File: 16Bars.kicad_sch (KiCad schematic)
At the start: 34 parts, among them IC1 CD4033BE, IC2 CD4033BE, IC3 CD4510BE, J1 CLOCK_IN, J2 Conn_02x05_Odd_Even, Q1 2N3904, Q2 2N3904, Q3 2N3904, Q4 2N3904, Q5 2N3904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

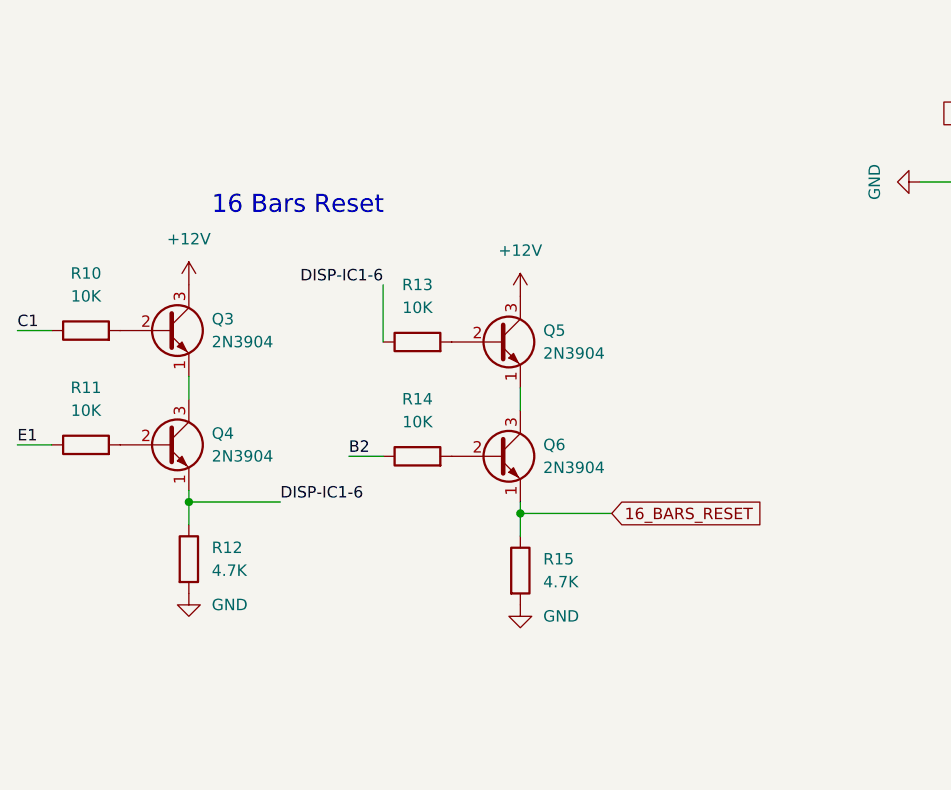
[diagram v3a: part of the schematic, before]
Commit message: Fix transistor logic. TODO resistor values.
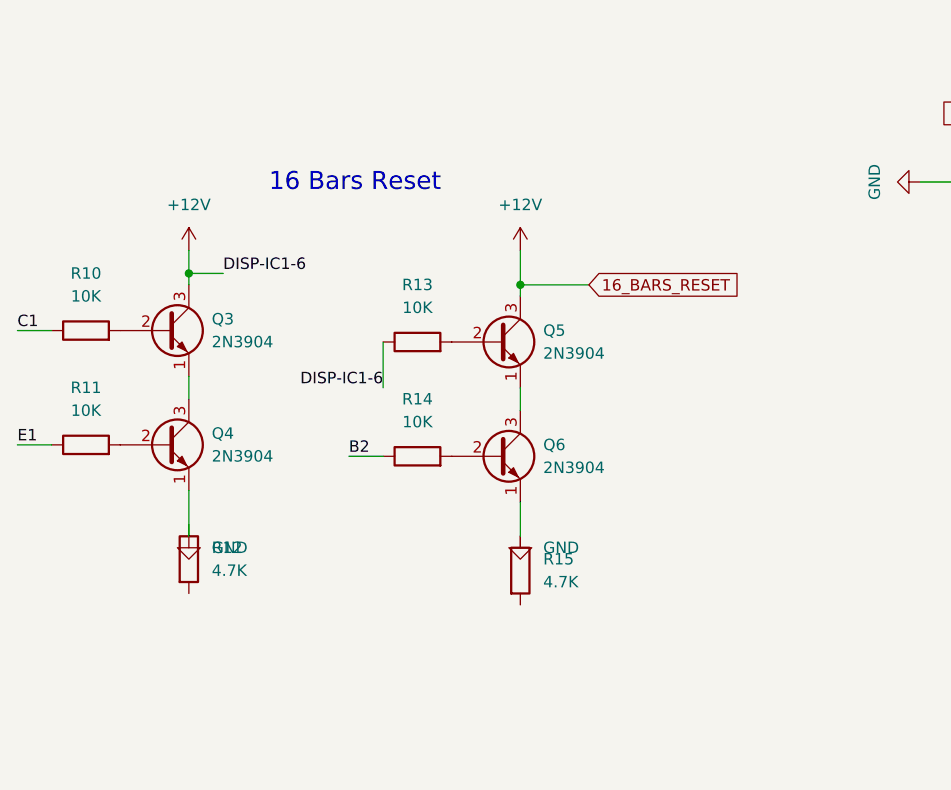
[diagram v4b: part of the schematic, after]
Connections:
- net +12V: now also IC1.15 (RESET), IC2.15 (RESET), IC3.9 (RESET), R13.1, R2.2, R4.2, R6.2, SW1.2
- net GND: now also Q4.1 (E), Q6.1 (E), R15.1; no longer R12.2, R15.2
- removed net 16_BARS_RESET: IC1.15 (RESET), IC2.15 (RESET), IC3.9 (RESET), Q6.1 (E), R15.1, R2.2, R4.2, R6.2, SW1.2
- removed net DISP-IC1-6: Q4.1 (E), R12.1, R13.1
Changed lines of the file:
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@@
   (junction (at 39.37 176.53) (diameter 0) (color 0 0 0 0)
   )
-  (junction (at 90.17 113.03) (diameter 0) (color 0 0 0 0)
-  )
   (junction (at 64.77 38.1) (diameter 0) (color 0 0 0 0)
   )
+  (junction (at 90.17 87.63) (diameter 0) (color 0 0 0 0)
+  )
   (junction (at 50.8 176.53) (diameter 0) (color 0 0 0 0)
   )
   (junction (at 198.12 22.86) (diameter 0) (color 0 0 0 0)
   )
+  (junction (at 53.34 86.36) (diameter 0) (color 0 0 0 0)
+  )
   (junction (at 198.12 33.02) (diameter 0) (color 0 0 0 0)
   )
@@
   )
   (junction (at 60.96 22.86) (diameter 0) (color 0 0 0 0)
-  )
-  (junction (at 53.34 111.76) (diameter 0) (color 0 0 0 0)
   )
   (junction (at 39.37 171.45) (diameter 0) (color 0 0 0 0)
@@
     (stroke (width 0) (type default) (color 0 0 0 0))
   )
+  (wire (pts (xy 90.17 83.82) (xy 90.17 87.63))
+    (stroke (width 0) (type default) (color 0 0 0 0))
+  )
   (wire (pts (xy 110.49 35.56) (xy 118.11 35.56))
     (stroke (width 0) (type default) (color 0 0 0 0))
@@
     (stroke (width 0) (type default) (color 0 0 0 0))
   )
-  (wire (pts (xy 90.17 113.03) (xy 100.33 113.03))
-    (stroke (width 0) (type default) (color 0 0 0 0))
-  )
   (wire (pts (xy 201.93 69.85) (xy 204.47 69.85))
     (stroke (width 0) (type default) (color 0 0 0 0))
@@
     (stroke (width 0) (type default) (color 0 0 0 0))
   )
+  (wire (pts (xy 90.17 87.63) (xy 90.17 88.9))
+    (stroke (width 0) (type default) (color 0 0 0 0))
+  )
+  (wire (pts (xy 90.17 87.63) (xy 97.79 87.63))
+    (stroke (width 0) (type default) (color 0 0 0 0))
+  )
   (wire (pts (xy 26.67 179.07) (xy 26.67 176.53))
     (stroke (width 0) (type default) (color 0 0 0 0))
@@
     (stroke (width 0) (type default) (color 0 0 0 0))
   )
-  (wire (pts (xy 74.93 87.63) (xy 74.93 93.98))
+  (wire (pts (xy 74.93 99.06) (xy 74.93 93.98))
     (stroke (width 0) (type default) (color 0 0 0 0))
   )
@@
     (stroke (width 0) (type default) (color 0 0 0 0))
   )
-  (wire (pts (xy 90.17 113.03) (xy 90.17 111.76))
+  (wire (pts (xy 90.17 111.76) (xy 90.17 115.57))
     (stroke (width 0) (type default) (color 0 0 0 0))
   )
@@
     (stroke (width 0) (type default) (color 0 0 0 0))
   )
-  (wire (pts (xy 53.34 114.3) (xy 53.34 111.76))
-    (stroke (width 0) (type default) (color 0 0 0 0))
-  )
-  (wire (pts (xy 53.34 111.76) (xy 63.5 111.76))
-    (stroke (width 0) (type default) (color 0 0 0 0))
-  )
-  (wire (pts (xy 90.17 115.57) (xy 90.17 113.03))
+  (wire (pts (xy 53.34 110.49) (xy 53.34 115.57))
     (stroke (width 0) (type default) (color 0 0 0 0))
   )
@@
     (stroke (width 0) (type default) (color 0 0 0 0))
   )
-  (wire (pts (xy 53.34 111.76) (xy 53.34 110.49))
+  (wire (pts (xy 53.34 86.36) (xy 53.34 87.63))
     (stroke (width 0) (type default) (color 0 0 0 0))
   )
@@
     (stroke (width 0) (type default) (color 0 0 0 0))
   )
+  (wire (pts (xy 53.34 86.36) (xy 57.15 86.36))
+    (stroke (width 0) (type default) (color 0 0 0 0))
+  )
   (wire (pts (xy 146.05 33.02) (xy 147.32 33.02))
     (stroke (width 0) (type default) (color 0 0 0 0))
@@
   )
   (wire (pts (xy 58.42 22.86) (xy 60.96 22.86))
+    (stroke (width 0) (type default) (color 0 0 0 0))
+  )
+  (wire (pts (xy 53.34 83.82) (xy 53.34 86.36))
     (stroke (width 0) (type default) (color 0 0 0 0))
   )
@@
     (effects (font (size 2 2)) (justify right bottom))
   )
-  (text "16 Bars Reset\n" (at 55.88 80.01 0)
+  (text "16 Bars Reset\n" (at 62.23 77.47 0)
     (effects (font (size 2 2)) (justify left bottom))
   )
@@
     (effects (font (size 1.27 1.27)) (justify left bottom))
   )
-  (label "DISP-IC1-6" (at 74.93 87.63 180)
+  (label "DISP-IC1-6" (at 74.93 99.06 180)
     (effects (font (size 1.27 1.27)) (justify right bottom))
   )
@@
     (effects (font (size 1.27 1.27)) (justify left bottom))
   )
-  (label "DISP-IC1-6" (at 63.5 111.76 0)
+  (label "DISP-IC1-6" (at 57.15 86.36 0)
     (effects (font (size 1.27 1.27)) (justify left bottom))
   )
@@
     )
   )
-  (global_label "16_BARS_RESET" (shape input) (at 100.33 113.03 0) (fields_autoplaced)
+  (global_label "16_BARS_RESET" (shape input) (at 97.79 87.63 0) (fields_autoplaced)
     (effects (font (size 1.27 1.27)) (justify left))
-    (property "Intersheet References" "${INTERSHEET_REFS}" (id 0) (at 117.6807 112.9506 0)
+    (property "Intersheet References" "${INTERSHEET_REFS}" (id 0) (at 115.1407 87.5506 0)
       (effects (font (size 1.27 1.27)) (justify left) hide)
     )
@@
     (pin "1")
   )
-  (symbol (lib_id "power:+12V") (at 53.34 87.63 0) (unit 1)
-    (in_bom yes) (on_board yes) (fields_autoplaced)
-    (property "Reference" "#PWR03" (id 0) (at 53.34 91.44 0)
-      (effects (font (size 1.27 1.27)) hide)
-    )
-    (property "Value" "+12V" (id 1) (at 53.34 82.55 0))
-    (property "Footprint" "" (id 2) (at 53.34 87.63 0)
-      (effects (font (size 1.27 1.27)) hide)
-    )
-    (property "Datasheet" "" (id 3) (at 53.34 87.63 0)
+  (symbol (lib_id "power:+12V") (at 53.34 83.82 0) (unit 1)
+    (in_bom yes) (on_board yes) (fields_autoplaced)
+    (property "Reference" "#PWR03" (id 0) (at 53.34 87.63 0)
+      (effects (font (size 1.27 1.27)) hide)
+    )
+    (property "Value" "+12V" (id 1) (at 53.34 78.74 0))
+    (property "Footprint" "" (id 2) (at 53.34 83.82 0)
+      (effects (font (size 1.27 1.27)) hide)
+    )
+    (property "Datasheet" "" (id 3) (at 53.34 83.82 0)
       (effects (font (size 1.27 1.27)) hide)
     )
@@
     (pin "2")
   )
-  (symbol (lib_id "power:+12V") (at 90.17 88.9 0) (unit 1)
-    (in_bom yes) (on_board yes) (fields_autoplaced)
-    (property "Reference" "#PWR023" (id 0) (at 90.17 92.71 0)
-      (effects (font (size 1.27 1.27)) hide)
-    )
-    (property "Value" "+12V" (id 1) (at 90.17 83.82 0))
-    (property "Footprint" "" (id 2) (at 90.17 88.9 0)
-      (effects (font (size 1.27 1.27)) hide)
-    )
-    (property "Datasheet" "" (id 3) (at 90.17 88.9 0)
+  (symbol (lib_id "power:+12V") (at 90.17 83.82 0) (unit 1)
+    (in_bom yes) (on_board yes) (fields_autoplaced)
+    (property "Reference" "#PWR023" (id 0) (at 90.17 87.63 0)
+      (effects (font (size 1.27 1.27)) hide)
+    )
+    (property "Value" "+12V" (id 1) (at 90.17 78.74 0))
+    (property "Footprint" "" (id 2) (at 90.17 83.82 0)
+      (effects (font (size 1.27 1.27)) hide)
+    )
+    (property "Datasheet" "" (id 3) (at 90.17 83.82 0)
       (effects (font (size 1.27 1.27)) hide)
     )
@@
     (pin "1")
   )
-  (symbol (lib_id "power:GND") (at 53.34 121.92 0) (unit 1)
-    (in_bom yes) (on_board yes) (fields_autoplaced)
-    (property "Reference" "#PWR022" (id 0) (at 53.34 128.27 0)
-      (effects (font (size 1.27 1.27)) hide)
-    )
-    (property "Value" "GND" (id 1) (at 55.88 123.1899 0)
-      (effects (font (size 1.27 1.27)) (justify left))
-    )
-    (property "Footprint" "" (id 2) (at 53.34 121.92 0)
-      (effects (font (size 1.27 1.27)) hide)
-    )
-    (property "Datasheet" "" (id 3) (at 53.34 121.92 0)
+  (symbol (lib_id "power:GND") (at 53.34 115.57 0) (unit 1)
+    (in_bom yes) (on_board yes) (fields_autoplaced)
+    (property "Reference" "#PWR022" (id 0) (at 53.34 121.92 0)
+      (effects (font (size 1.27 1.27)) hide)
+    )
+    (property "Value" "GND" (id 1) (at 55.88 116.8399 0)
+      (effects (font (size 1.27 1.27)) (justify left))
+    )
+    (property "Footprint" "" (id 2) (at 53.34 115.57 0)
+      (effects (font (size 1.27 1.27)) hide)
+    )
+    (property "Datasheet" "" (id 3) (at 53.34 115.57 0)
       (effects (font (size 1.27 1.27)) hide)
     )
@@
     (pin "1")
   )
-  (symbol (lib_id "power:GND") (at 90.17 123.19 0) (unit 1)
-    (in_bom yes) (on_board yes) (fields_autoplaced)
-    (property "Reference" "#PWR024" (id 0) (at 90.17 129.54 0)
-      (effects (font (size 1.27 1.27)) hide)
-    )
-    (property "Value" "GND" (id 1) (at 92.71 124.4599 0)
-      (effects (font (size 1.27 1.27)) (justify left))
-    )
-    (property "Footprint" "" (id 2) (at 90.17 123.19 0)
-      (effects (font (size 1.27 1.27)) hide)
-    )
-    (property "Datasheet" "" (id 3) (at 90.17 123.19 0)
-      (effects (font (size 1.27 1.27)) hide)
-    )
+  (symbol (lib_id "power:GND") (at 90.17 115.57 0) (unit 1)
+    (in_bom yes) (on_board yes) (fields_autoplaced)
+    (property "Reference" "#PWR024" (id 0) (at 90.17 121.92 0)
+      (effects (font (size 1.27 1.27)) hide)
+    )
+    (property "Value" "GND" (id 1) (at 92.71 116.8399 0)
+      (effects (font (size 1.27 1.27)) (justify left))
+    )
+    (property "Footprint" "" (id 2) (at 90.17 115.57 0)
+      (effects (font (size 1.27 1.27)) hide)
+    )
+    (property "Datasheet" "" (id 3) (at 90.17 115.57 0)
+      (effects (font (size 1.27 1.27)) hide)
+    )

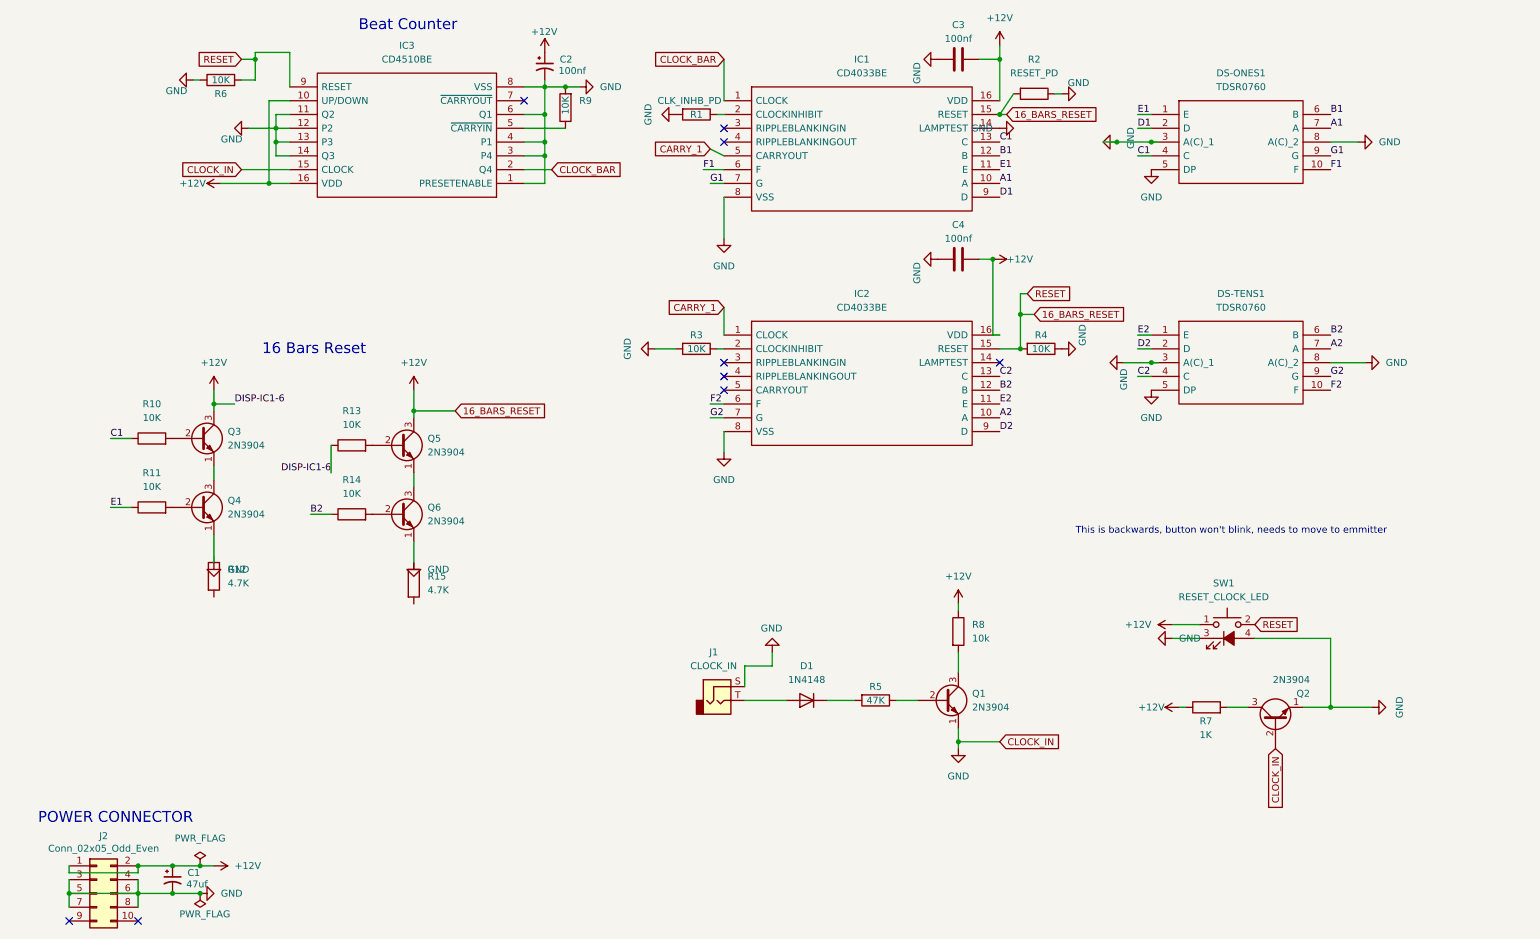
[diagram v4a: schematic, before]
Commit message: Update PCB and Schematic Footprints
Better 7Seg layout
Update 7seg footprint
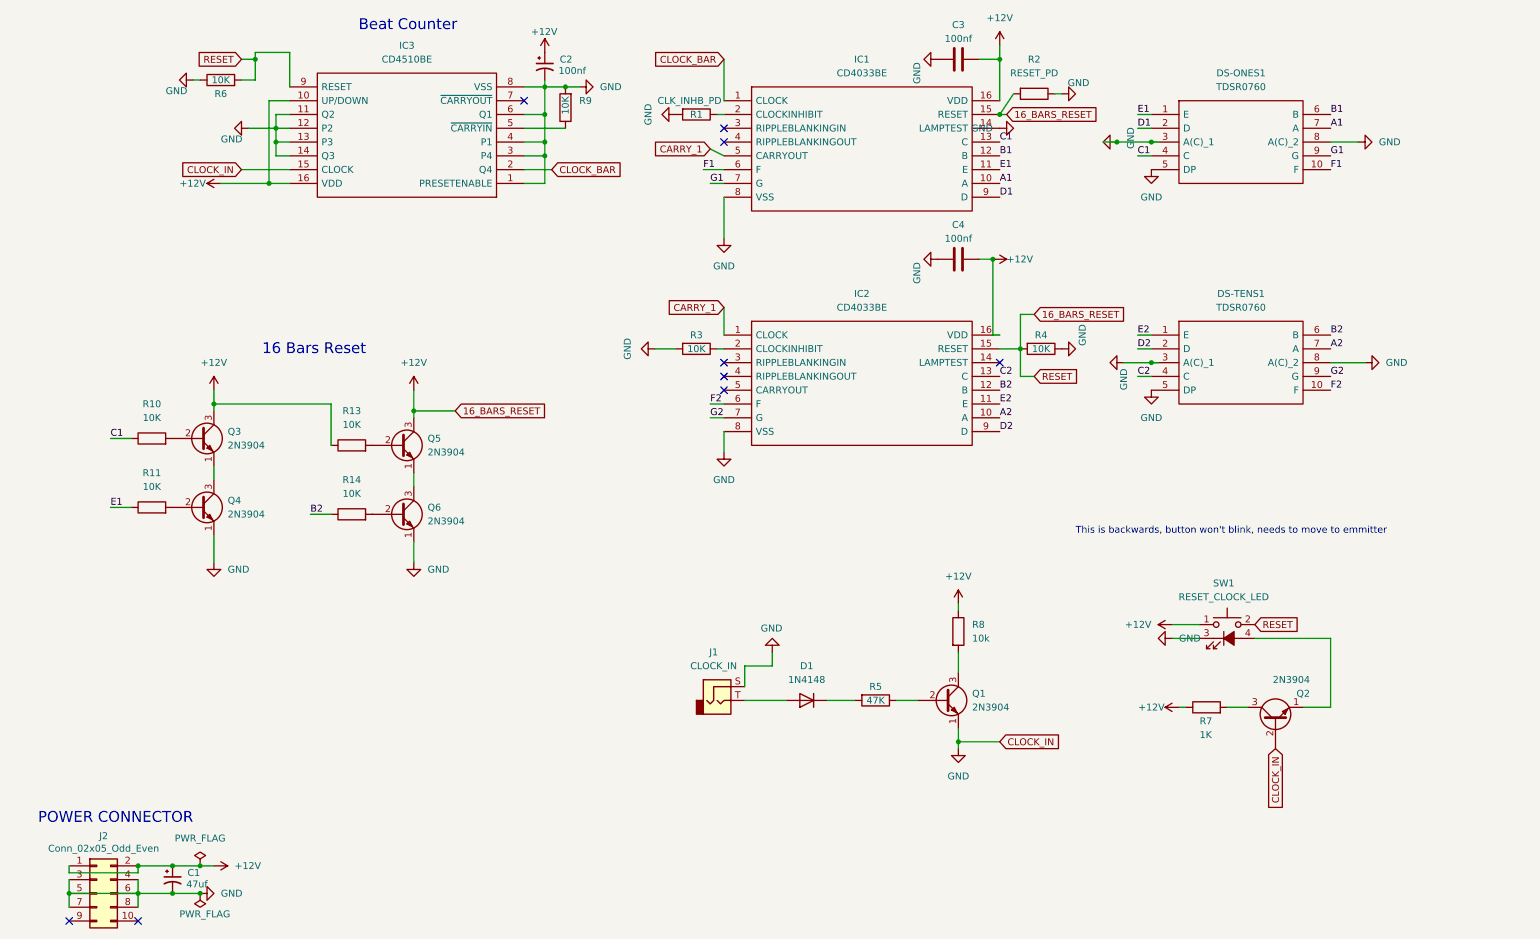
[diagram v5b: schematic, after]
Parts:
- removed R12, R15: 4.7K, Resistor_THT:R_Axial_DIN0204_L3.6mm_D1.6mm_P5.08mm_Horizontal, symbol Device:R
- C2, C3, C4: footprint Capacitor_THT:C_Disc_D7.0mm_W2.5mm_P5.00mm -> Capacitor_SMD:C_0402_1005Metric
- DS-ONES1, DS-TENS1: footprint SamacSys_Parts:TDSR0760 -> TDSR*:TDSR0760
- R1, R10, R11, R13, R14, R2, R3, R4, R5, R6, R7, R8, R9: footprint Resistor_THT:R_Axial_DIN0204_L3.6mm_D1.6mm_P5.08mm_Horizontal -> Resistor_SMD:R_0402_1005Metric
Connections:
- net GND: no longer Q2.1 (E), SW1.4 (A)
- new net: Q2.1 (E), SW1.4 (A)

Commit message: Add Thonk Low Profile LED Button Symbol
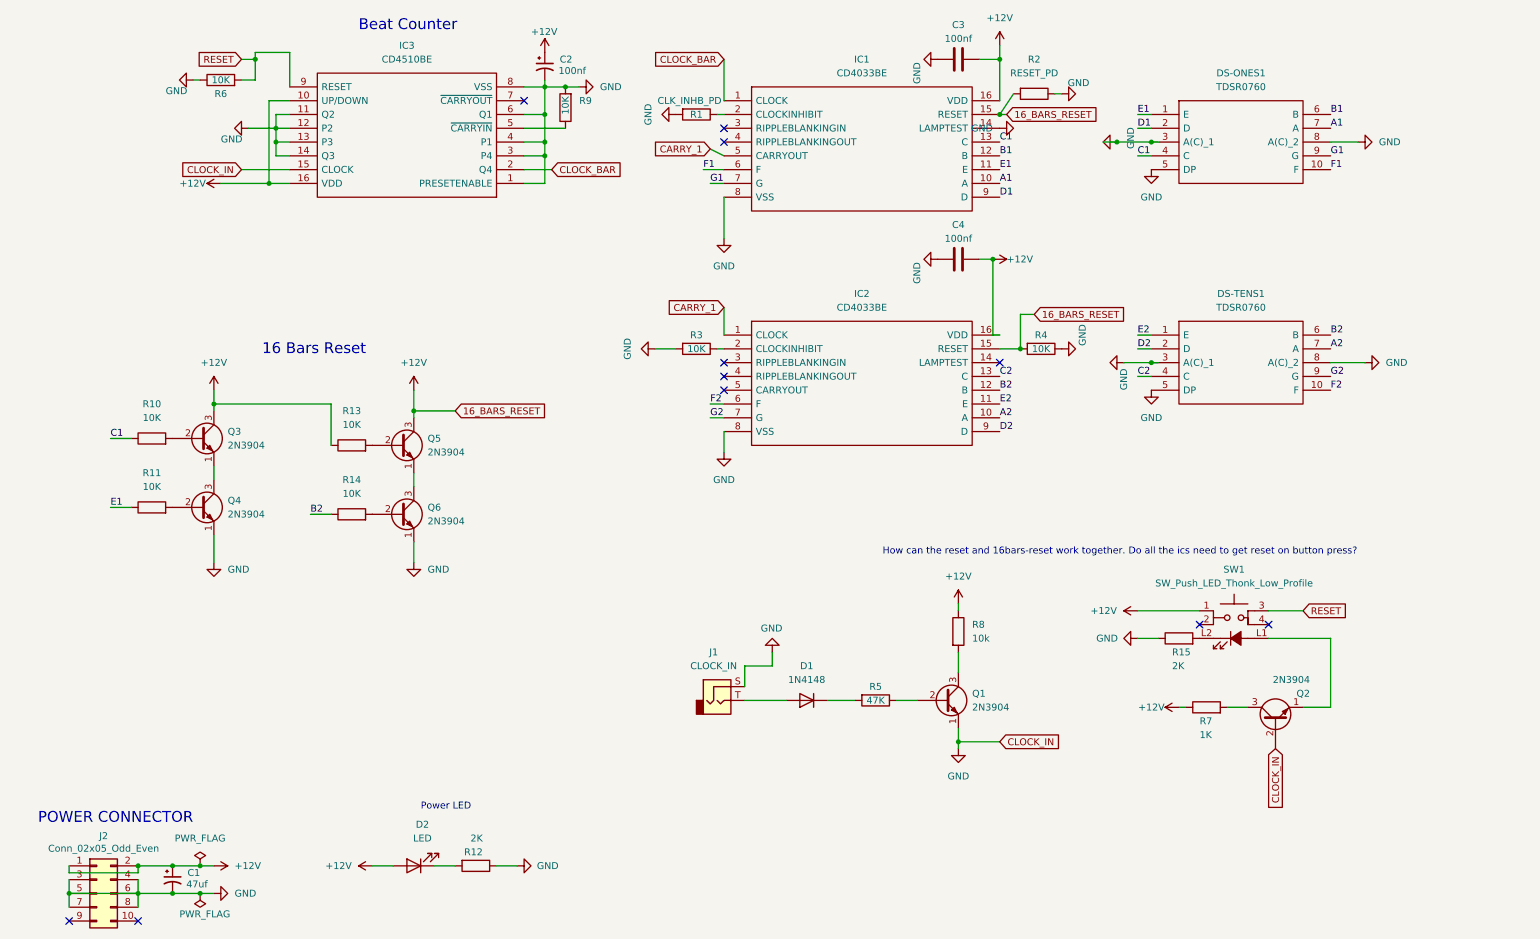
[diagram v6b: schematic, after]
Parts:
- removed SW1: RESET_CLOCK_LED, Button_Switch_THT:Thonk-LED-Button-MomentaryON, symbol Switch:SW_Push_LED
- added D2: LED, symbol Device:LED
- added R12, R15: 2K, Resistor_SMD:R_0402_1005Metric, symbol Device:R
- added SW1: SW_Push_LED_Thonk_Low_Profile, Button_Switch_THT:Thonk-LED-Button-MomentaryON, symbol TDSR*:SW_Push_LED_Thonk_Low_Profile
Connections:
- net +12V: now also D2.2 (A), SW1.1; no longer IC3.9 (RESET), R6.2
- net GND: now also R12.1, R15.1
- net at Q2.1 (E): now also SW1.L1
- new net: R15.2, SW1.L2
- new net: D2.1 (K), R12.2
- new net RESET: IC3.9 (RESET), R6.2, SW1.3
- no-connect marks 9 -> 11
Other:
- note added: "How can the reset and 16bars-reset work together. Do all the ics need to get reset on button press?"
- note added: "Power LED"
- note removed: "This is backwards, button won't blink, needs to move to emmitter"
